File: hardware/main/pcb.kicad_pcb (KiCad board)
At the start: 2 copper layers, 55 x 55 mm, 29 parts, among them J3 Conn_01x03_Socket, Q1 BC547, Q2 BC547, Q3 BC547, U1 ESP32 C3 supper mini

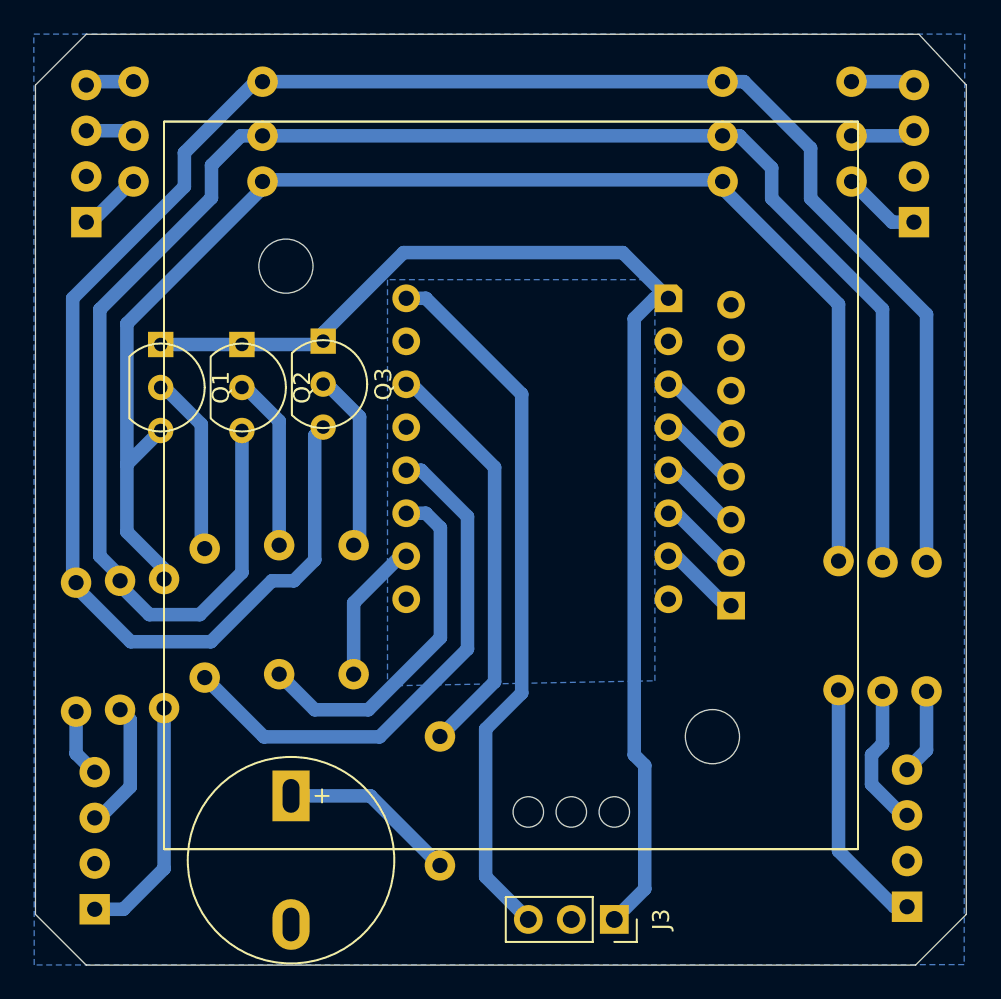
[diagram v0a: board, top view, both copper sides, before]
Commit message: Migrate PCB to addressable LEDs, 42x42 mm single-layer board
- Resize board to 42x42 mm with chamfered corners, 1.6 mm thickness
- Move LEDs and JST connector to fit; add GND pointer to LED footprints
- Replace pin socket with 2.54 mm JST footprint with built-in pin labels
- Re-route traces on the back copper layer only
- Move all text to the solder-side silkscreen, drop PN532 silkscreen
- Move libraries to hardware/libs and remove unused footprints/models

Co-Authored-By: Claude Sonnet 5.5 <noreply@anthropic.com>
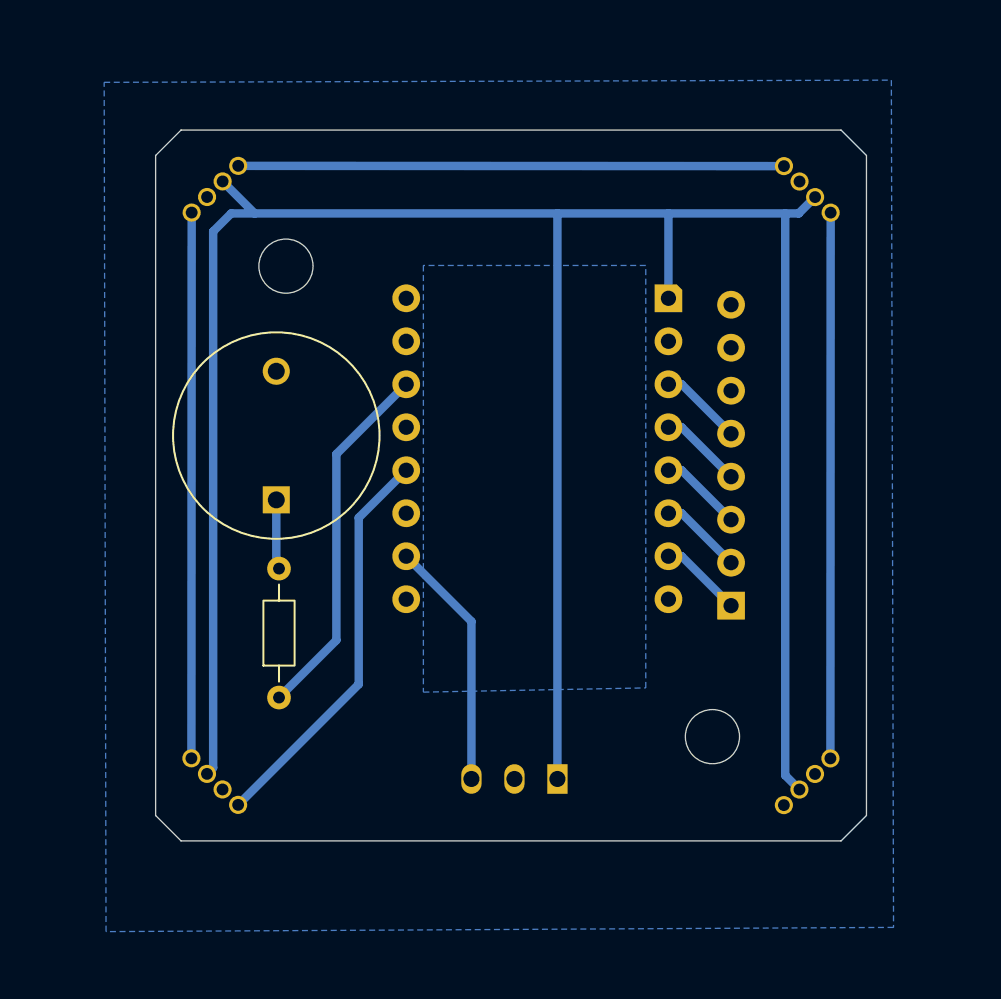
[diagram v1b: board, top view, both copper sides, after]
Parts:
- removed Q1, Q2, Q3: BC547, Package_TO_SOT_THT:TO-92_Inline
- removed the R1 at (113.4, 48.7)
- removed R10, R11, R2, R3, R4, R5, R7, R8: 100, Resistor_THT:CNC_Ready_R_Axial_DIN0204_L3.6mm_D1.6mm_P7.62mm_Horizontal
- removed R12, R6, R9: 150, Resistor_THT:CNC_Ready_R_Axial_DIN0204_L3.6mm_D1.6mm_P7.62mm_Horizontal
- removed R14, R15, R16: 1000, Resistor_THT:CNC_Ready_R_Axial_DIN0204_L3.6mm_D1.6mm_P7.62mm_Horizontal
- BZ1: footprint Buzzer_Beeper:MagneticBuzzer_ProSignal_ABI-010-RC -> prismo:MagneticBuzzer_ProSignal_ABI-010-RC
- D1, D2, D3, D4: value LED_RKGB -> WS2812B; footprint LED_THT:LED_D5.0mm-4_RGB_Wide_Pins_CNC_read -> prismo:LED_D5.0mm-2812-D-diagonal
- J3: footprint Connector_PinSocket_2.54mm:PinSocket_1x03_P2.54mm_Vertical_with_holes -> prismo:JST_1x03_P2.54mm_Vertical
- R1: renamed from R13; footprint Resistor_THT:CNC_Ready_R_Axial_DIN0204_L3.6mm_D1.6mm_P7.62mm_Horizontal -> prismo:R_Axial_DIN0204_L3.6mm_D1.6mm_P7.62mm_Horizontal
- REF** (x2): footprint MountingHole:MountingHole_3.2mm_M3_DIN965 -> prismo:MountingHole_3.2mm_M3_DIN965
- U1: value ESP32 C3 supper mini -> ~; footprint esp_32_c3_supper_mini:esp_32_c3_supper_mini -> prismo:esp_32_c3_supper_mini
- U2: footprint esp_32_c3_supper_mini:PN532 NFC RFID simple (one row) -> prismo:PN532 NFC RFID simple (one row)
- moved D3 61.2 mm to (147.5, 49.2), turned to 180 degrees
- moved D2 41.5 mm to (110.6, 47.3), turned to -90 degrees
- moved D1 33.5 mm to (108.7, 84.2), turned to 0 degrees
- moved BZ1 17.5 mm to (114.2, 67.5), turned to 90 degrees
- moved R1 9.78 mm to (114.4, 79.2), turned to 90 degrees
- moved J3 8.95 mm to (130.8, 84.0), turned to 180 degrees
- moved D4 8.06 mm to (145.6, 86.1)
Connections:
- D1 pad 1: Net-(D1-RA) -> Net-(D1-DOUT)
- D1 pad 2: GND -> +5V
- D1 pad 3: Net-(D1-GA) -> GND
- D1 pad 4: Net-(D1-BA) -> Net-(D1-DIN)
- D2 pad 1: Net-(D2-RA) -> Net-(D2-DOUT)
- D2 pad 2: GND -> +5V
- D2 pad 3: Net-(D2-GA) -> GND
- D2 pad 4: Net-(D2-BA) -> Net-(D1-DOUT)
- D3 pad 1: Net-(D3-RA) -> Net-(D3-DOUT)
- D3 pad 2: GND -> +5V
- D3 pad 3: Net-(D3-GA) -> GND
- D3 pad 4: Net-(D3-BA) -> Net-(D2-DOUT)
- D4 pad 1: Net-(D4-RA) -> unconnected-(D4-DOUT-Pad1)
- D4 pad 2: GND -> +5V
- D4 pad 3: Net-(D4-GA) -> GND
- D4 pad 4: Net-(D4-BA) -> Net-(D3-DOUT)
- U1 pad 13: /R -> Net-(D1-DIN)
- U1 pad 14: /G -> unconnected-(U1-GPIO10-Pad14)
- U1 pad 15: /B -> Net-(J3-Pin_3)
- U1 pad 9: Net-(J3-Pin_3) -> unconnected-(U1-GPIO5/MISO-Pad9)
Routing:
- net Net-(Q3-E): track 121.7 -> 0.00 mm
- net Net-(Q2-E): track 106.0 -> 0.00 mm
- net Net-(Q1-E): track 83.6 -> 0.00 mm
- net +5V: track 72.7 -> 144.1 mm
- net Net-(D1-DOUT): track 0.00 -> 32.2 mm
- net Net-(D3-DOUT): track 0.00 -> 32.2 mm
- net Net-(D2-DOUT): track 0.00 -> 32.2 mm
- net /R: track 31.7 -> 0.00 mm
- net Net-(J3-Pin_3): track 42.1 -> 14.8 mm
- net Net-(D1-DIN): track 0.00 -> 23.9 mm
- net /G: track 21.0 -> 0.00 mm
- net Net-(D4-RA): track 14.9 -> 0.00 mm
- net Net-(D3-RA): track 14.6 -> 0.00 mm
- net Net-(Q3-B): track 10.4 -> 0.00 mm
- net Net-(Q1-B): track 10.0 -> 0.00 mm
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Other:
- board size 55 x 55 mm -> 42 x 42 mm
- board text added: "Prismo 1.0.0-RC.2"
- board text removed: "+"
- board text removed: "+5V"
- board text removed: "GND"
- board text removed: "Prismo 1.0.0-RC.1"
- board text removed: "RKGB"
- board text removed: "SIGNAL"
